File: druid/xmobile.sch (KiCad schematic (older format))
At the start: 33 parts, among them CON1 AVR-PDI-6, IC1 ATXMEGA128A4U-A, P1 CONN_4_miniUSB, P2 CONN_1, P3 CONN_8, P6 CONN_10, P7 CONN_4, Q1 A2SHB, Q2 A2SHB, SW1 SW_PUSH, U1 STF202-22T1G, U2 SIM800C

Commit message: - Переделана клавиатура - установлены все корпуса микросхем
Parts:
- removed P1: CONN_4_miniUSB, symbol CONN_4
- removed SW1: SW_PUSH, symbol SW_PUSH
- added P1: USB_B, usb:Conn_USBmicro-B_ebay-side_TH, symbol USB_B
- added U5: switch1, symbol switch1
- C1, C3: footprint (none) -> Capacitors_SMD:C_1206_HandSoldering; symbol C -> C-RESCUE-xmobile
- C2: footprint (none) -> Capacitors_SMD:c_elec_4x5.3; symbol CP1 -> CP1-RESCUE-xmobile
- D1: footprint (none) -> LEDs:LED_0603; symbol LED -> LED-RESCUE-xmobile
- IC1: symbol ATXMEGA128A4U-A -> ATXMEGA128A4U-A-RESCUE-xmobile
- L1: footprint (none) -> Inductors:Inductor_1212
- P3: footprint (none) -> Connectors_Molex:Molex_KK-6410-08_08x2.54mm_Straight
- P6: footprint (none) -> Connectors_Molex:Molex_KK-6410-06_06x2.54mm_Straight
- P7: footprint (none) -> Connectors_Molex:Molex_KK-6410-04_04x2.54mm_Straight
- R1, R2, R6: footprint Resistors_SMD:R_0402 -> Resistors_SMD:R_0603_HandSoldering; symbol R -> R-RESCUE-xmobile
- R10, R11, R12, R13, R14, R15, R16, R7, R8, R9: footprint (none) -> Resistors_SMD:R_0603_HandSoldering; symbol R -> R-RESCUE-xmobile
- R3, R4, R5: footprint Resistors_SMD:R_0402 -> Resistors_SMD:R_0603; symbol R -> R-RESCUE-xmobile
- U1: footprint MODULE -> semiconductor:TSOP-6
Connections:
- no-connect marks 1 -> 4

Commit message: Исправлины все ошибки и предупреждения в электрической схеме
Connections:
- net labels added: SIM_HOLDER_VDD_EXT
- net labels removed: GSM_VDD_EXT, XMEGA_RESET
- wire segments 41 -> 42
- no-connect marks 4 -> 13
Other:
- moved on the sheet: CON1, R6, U5
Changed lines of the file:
@@
 L R-RESCUE-xmobile R6
 U 1 1 5967CB22
-P 14100 4200
-F 0 "R6" V 14180 4200 40  0000 C CNN
-F 1 "10k" V 14107 4201 40  0000 C CNN
-F 2 "Resistors_SMD:R_0603_HandSoldering" V 14030 4200 30  0001 C CNN
-F 3 "" H 14100 4200 30  0000 C CNN
-	1    14100 4200
+P 14375 4725
+F 0 "R6" V 14455 4725 40  0000 C CNN
+F 1 "10k" V 14382 4726 40  0000 C CNN
+F 2 "Resistors_SMD:R_0603_HandSoldering" V 14305 4725 30  0001 C CNN
+F 3 "" H 14375 4725 30  0000 C CNN
+	1    14375 4725
 	-1   0    0    1
 $EndComp
@@
 Text Label 11200 7225 0    60   ~ 0
 GND
-Text Label 14100 3950 2    60   ~ 0
+Text Label 14375 4475 2    60   ~ 0
 3.3V
 $Comp
@@
 Text Label 9500 7675 2    60   ~ 0
 SIM_VDD
-Text Label 11200 6550 0    60   ~ 0
-GSM_VDD_EXT
 NoConn ~ 11200 6700
 Text Label 11200 7150 0    60   ~ 0
@@
 L AVR-PDI-6 CON1
 U 1 1 5AA047A2
-P 14650 4575
-F 0 "CON1" H 14570 4815 50  0000 C CNN
-F 1 "AVR-PDI-6" H 14440 4330 50  0000 L BNN
-F 2 "AVR-PDI-6" V 14205 4610 50  0001 C CNN
-F 3 "" H 14650 4575 60  0001 C CNN
-	1    14650 4575
-	1    0    0    -1
-$EndComp
-Text Label 14525 4675 2    60   ~ 0
-PDI_C
-Text Label 14775 4475 0    60   ~ 0
+P 14925 5100
+F 0 "CON1" H 14845 5340 50  0000 C CNN
+F 1 "AVR-PDI-6" H 14715 4855 50  0000 L BNN
+F 2 "AVR-PDI-6" V 14480 5135 50  0001 C CNN
+F 3 "" H 14925 5100 60  0001 C CNN
+	1    14925 5100
+	1    0    0    -1
+$EndComp
+Text Label 15050 5000 0    60   ~ 0
 3.3V
-Text Label 14775 4675 0    60   ~ 0
+Text Label 15050 5200 0    60   ~ 0
 GND
 Text Label 9000 2700 2    60   ~ 0
 PDI_D
 Wire Wire Line
-	14100 4450 14100 4925
-Wire Wire Line
-	13950 4475 14525 4475
+	14375 4975 14375 5450
 Text Label 8900 2600 2    60   ~ 0
-XMEGA_RESET
-Text Label 13950 4475 2    60   ~ 0
-XMEGA_RESET
-Connection ~ 14100 4475
-Text Label 13900 5625 3    60   ~ 0
+PDI_C
+Text Label 14175 6150 3    60   ~ 0
 GND
 $Sheet
@@
 L switch1 U5
 U 1 1 5AB790A5
-P 14000 5275
-F 0 "U5" H 14000 5075 60  0000 C CNN
-F 1 "switch1" H 14000 5475 60  0000 C CNN
-F 2 "" H 14000 5275 60  0001 C CNN
-F 3 "" H 14000 5275 60  0001 C CNN
-	1    14000 5275
-	0    1    1    0
-$EndComp
-Text Label 14000 5625 3    60   ~ 0
-GND
-NoConn ~ 14100 5625
-NoConn ~ 13900 4925
+P 14275 5800
+F 0 "U5" H 14275 5600 60  0000 C CNN
+F 1 "switch1" H 14275 6000 60  0000 C CNN
+F 2 "" H 14275 5800 60  0001 C CNN
+F 3 "" H 14275 5800 60  0001 C CNN
+	1    14275 5800
+	0    1    1    0
+$EndComp
+Text Label 14275 6150 3    60   ~ 0
+GND
+NoConn ~ 14375 6150
+NoConn ~ 14175 5450
 $Comp
 L USB_B P1
@@
 GND
 NoConn ~ 12975 4050
+NoConn ~ 15050 5100
+NoConn ~ 14800 5100
+Wire Wire Line
+	14225 5200 14800 5200
+Connection ~ 14375 5200
+Text Label 14800 5000 2    60   ~ 0
+PDI_D
+Text Label 14225 5200 2    60   ~ 0
+PDI_C
+$Comp
+L PWR_FLAG #FLG01
+U 1 1 5AB82AA2
+P 3050 1350
+F 0 "#FLG01" H 3050 1445 50  0001 C CNN
+F 1 "PWR_FLAG" H 3050 1530 50  0000 C CNN
+F 2 "" H 3050 1350 50  0000 C CNN
+F 3 "" H 3050 1350 50  0000 C CNN
+	1    3050 1350
+	1    0    0    -1
+$EndComp
+Wire Wire Line
+	2725 1350 3050 1350
+$Comp
+L PWR_FLAG #FLG02
+U 1 1 5AB83225
+P 10200 1500
+F 0 "#FLG02" H 10200 1595 50  0001 C CNN
+F 1 "PWR_FLAG" H 10200 1680 50  0000 C CNN
+F 2 "" H 10200 1500 50  0000 C CNN
+F 3 "" H 10200 1500 50  0000 C CNN
+	1    10200 1500
+	1    0    0    -1
+$EndComp
+NoConn ~ 11200 6400
+Text Label 11200 6850 0    60   ~ 0
+GND
+NoConn ~ 11200 7375
+NoConn ~ 11200 7450
+NoConn ~ 11200 7825
+NoConn ~ 11200 7900
+NoConn ~ 9500 7825
+NoConn ~ 9000 3550
+Text Label 3275 9525 0    60   ~ 0
+SIM_DET
+Text Label 2225 9425 2    60   ~ 0
+SIM_DATA
+Text Label 3275 9225 0    60   ~ 0
+SIM_CLK
+Text Label 2225 9325 2    60   ~ 0
+SIM_RST
+Text Label 2225 9225 2    60   ~ 0
+SIM_VDD
+Text Label 3275 9325 0    60   ~ 0
+GND
+Text Label 11200 6550 0    60   ~ 0
+SIM_HOLDER_VDD_EXT
+Text Label 3275 9425 0    60   ~ 0
+SIM_HOLDER_VDD_EXT
 $EndSCHEMATC

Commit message: Переместил посадочные места по кучкам
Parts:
- removed P2: CONN_1, symbol CONN_1
- added P2: CONN_01X02, Connectors_Hirose:Hirose_DF13-02P-1.25DS_02x1.25mm_Angled, symbol CONN_01X02
- CON1: footprint AVR-PDI-6 -> Connectors_JAE:JAE_LY20-06P-2T_2x03x2.00mm_Straight
- IC1: footprint TQFP44 -> tqfp:TQFP-44_10x10mm_Pitch0.8mm
- P3: footprint Connectors_Molex:Molex_KK-6410-08_08x2.54mm_Straight -> Connectors_JAE:JAE_LY20-08P-2T_2x04x2.00mm_Straight
- P6: footprint Connectors_Molex:Molex_KK-6410-06_06x2.54mm_Straight -> Connectors_Hirose:Hirose_DF13-10P-1.25DSA_10x1.25mm_Straight
- P7: footprint Connectors_Molex:Molex_KK-6410-04_04x2.54mm_Straight -> Connectors_JAE:JAE_LY20-04P-2T_2x02x2.00mm_Straight
- R3, R4, R5: footprint Resistors_SMD:R_0603 -> Resistors_SMD:R_0603_HandSoldering
- U2: footprint SIM800C:SIM800C -> SIM800C_lup:SIM800C
- U5: footprint (none) -> switch1:switch_6x9
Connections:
- no-connect marks 13 -> 14
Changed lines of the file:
@@
 F 0 "U2" H 10600 8175 60  0000 C CNN
 F 1 "SIM800C" H 9900 8175 60  0000 C CNN
-F 2 "SIM800C:SIM800C" H 10375 7400 60  0000 C CNN
+F 2 "SIM800C_lup:SIM800C" H 10375 7400 60  0000 C CNN
 F 3 "" H 10550 7200 60  0000 C CNN
 	1    10550 7200
@@
 F 0 "IC1" H 9200 4750 50  0000 L BNN
 F 1 "ATXMEGA128A4U-A" H 10150 2400 50  0000 L BNN
-F 2 "TQFP44" H 9350 2450 50  0001 C CNN
+F 2 "tqfp:TQFP-44_10x10mm_Pitch0.8mm" H 9350 2450 50  0001 C CNN
 F 3 "" H 9900 3600 60  0001 C CNN
 	1    9900 3600
@@
 F 0 "P3" V 14475 1975 60  0000 C CNN
 F 1 "CONN_8" V 14575 1975 60  0000 C CNN
-F 2 "Connectors_Molex:Molex_KK-6410-08_08x2.54mm_Straight" H 14525 1975 60  0001 C CNN
+F 2 "Connectors_JAE:JAE_LY20-08P-2T_2x04x2.00mm_Straight" H 14525 1975 60  0001 C CNN
 F 3 "" H 14525 1975 60  0001 C CNN
 F 4 "EPD display connector" V 14700 1975 60  0000 C CNN "description"
@@
 F 0 "R3" V 6255 7100 40  0000 C CNN
 F 1 "4.7KOmh" V 6182 7101 40  0000 C CNN
-F 2 "Resistors_SMD:R_0603" V 6105 7100 30  0001 C CNN
+F 2 "Resistors_SMD:R_0603_HandSoldering" V 6105 7100 30  0001 C CNN
 F 3 "" H 6175 7100 30  0000 C CNN
 	1    6175 7100
@@
 F 0 "R5" V 6905 6550 40  0000 C CNN
 F 1 "470Ом" V 6832 6551 40  0000 C CNN
-F 2 "Resistors_SMD:R_0603" V 6755 6550 30  0001 C CNN
+F 2 "Resistors_SMD:R_0603_HandSoldering" V 6755 6550 30  0001 C CNN
 F 3 "" H 6825 6550 30  0000 C CNN
 	1    6825 6550
@@
 F 0 "R4" V 6555 7425 40  0000 C CNN
 F 1 "4.7KOmh" V 6482 7426 40  0000 C CNN
-F 2 "Resistors_SMD:R_0603" V 6405 7425 30  0001 C CNN
+F 2 "Resistors_SMD:R_0603_HandSoldering" V 6405 7425 30  0001 C CNN
 F 3 "" H 6475 7425 30  0000 C CNN
 	1    6475 7425
@@
 Text Label 11200 7150 0    60   ~ 0
 GSM_ANT
-Text Label 5525 1875 2    60   ~ 0
+Text Label 5500 2225 2    60   ~ 0
 GSM_ANT
-$Comp
-L CONN_1 P2
-U 1 1 5A9488D3
-P 5675 1875
-F 0 "P2" H 5755 1875 40  0000 L CNN
-F 1 "CONN_1" H 5675 1930 30  0001 C CNN
-F 2 "" H 5675 1875 60  0001 C CNN
-F 3 "" H 5675 1875 60  0001 C CNN
-	1    5675 1875
-	1    0    0    -1
-$EndComp
 Connection ~ 10200 1500
 Wire Wire Line
@@
 F 0 "CON1" H 14845 5340 50  0000 C CNN
 F 1 "AVR-PDI-6" H 14715 4855 50  0000 L BNN
-F 2 "AVR-PDI-6" V 14480 5135 50  0001 C CNN
+F 2 "Connectors_JAE:JAE_LY20-06P-2T_2x03x2.00mm_Straight" V 14480 5135 50  0001 C CNN
 F 3 "" H 14925 5100 60  0001 C CNN
 	1    14925 5100
@@
 F 0 "P6" V 13275 3050 60  0000 C CNN
 F 1 "CONN_10" V 13375 3050 60  0000 C CNN
-F 2 "Connectors_Molex:Molex_KK-6410-06_06x2.54mm_Straight" H 13325 3050 60  0001 C CNN
+F 2 "Connectors_Hirose:Hirose_DF13-10P-1.25DSA_10x1.25mm_Straight" H 13325 3050 60  0001 C CNN
 F 3 "" H 13325 3050 60  0001 C CNN
 	1    13325 3050
@@
 F 0 "P7" V 13275 3900 50  0000 C CNN
 F 1 "CONN_4" V 13375 3900 50  0000 C CNN
-F 2 "Connectors_Molex:Molex_KK-6410-04_04x2.54mm_Straight" H 13325 3900 60  0001 C CNN
+F 2 "Connectors_JAE:JAE_LY20-04P-2T_2x02x2.00mm_Straight" H 13325 3900 60  0001 C CNN
 F 3 "" H 13325 3900 60  0001 C CNN
 	1    13325 3900
@@
 F 0 "U5" H 14275 5600 60  0000 C CNN
 F 1 "switch1" H 14275 6000 60  0000 C CNN
-F 2 "" H 14275 5800 60  0001 C CNN
+F 2 "switch1:switch_6x9" H 14275 5800 60  0001 C CNN
 F 3 "" H 14275 5800 60  0001 C CNN
 	1    14275 5800
@@
 PDI_C
 $Comp
-L PWR_FLAG #FLG01
+L PWR_FLAG #FLG1
 U 1 1 5AB82AA2
 P 3050 1350
-F 0 "#FLG01" H 3050 1445 50  0001 C CNN
+F 0 "#FLG1" H 3050 1445 50  0001 C CNN
 F 1 "PWR_FLAG" H 3050 1530 50  0000 C CNN
 F 2 "" H 3050 1350 50  0000 C CNN
@@
 	2725 1350 3050 1350
 $Comp
-L PWR_FLAG #FLG02
+L PWR_FLAG #FLG2
 U 1 1 5AB83225
 P 10200 1500
-F 0 "#FLG02" H 10200 1595 50  0001 C CNN
+F 0 "#FLG2" H 10200 1595 50  0001 C CNN
 F 1 "PWR_FLAG" H 10200 1680 50  0000 C CNN
 F 2 "" H 10200 1500 50  0000 C CNN
@@
 Text Label 3275 9425 0    60   ~ 0
 SIM_HOLDER_VDD_EXT
+$Comp
+L CONN_01X02 P2
+U 1 1 5AB8506D
+P 5700 2275
+F 0 "P2" H 5700 2425 50  0000 C CNN
+F 1 "CONN_01X02" V 5800 2275 50  0000 C CNN
+F 2 "Connectors_Hirose:Hirose_DF13-02P-1.25DS_02x1.25mm_Angled" H 5700 2275 50  0000 C CNN
+F 3 "" H 5700 2275 50  0000 C CNN
+	1    5700 2275
+	1    0    0    -1
+$EndComp
+NoConn ~ 5500 2325
 $EndSCHEMATC

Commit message: Заменил посадочные места для некоторых контактных расчёсок
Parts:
- P6: footprint Connectors_Hirose:Hirose_DF13-10P-1.25DSA_10x1.25mm_Straight -> Connectors_JAE:JAE_LY20-08P-2T_2x04x2.00mm_Straight
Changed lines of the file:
@@
 F 0 "P6" V 13275 3050 60  0000 C CNN
 F 1 "CONN_10" V 13375 3050 60  0000 C CNN
-F 2 "Connectors_Hirose:Hirose_DF13-10P-1.25DSA_10x1.25mm_Straight" H 13325 3050 60  0001 C CNN
+F 2 "Connectors_JAE:JAE_LY20-08P-2T_2x04x2.00mm_Straight" H 13325 3050 60  0001 C CNN
 F 3 "" H 13325 3050 60  0001 C CNN
 	1    13325 3050
@@
 PDI_C
 $Comp
-L PWR_FLAG #FLG1
+L PWR_FLAG #FLG01
 U 1 1 5AB82AA2
 P 3050 1350
-F 0 "#FLG1" H 3050 1445 50  0001 C CNN
+F 0 "#FLG01" H 3050 1445 50  0001 C CNN
 F 1 "PWR_FLAG" H 3050 1530 50  0000 C CNN
 F 2 "" H 3050 1350 50  0000 C CNN
@@
 	2725 1350 3050 1350
 $Comp
-L PWR_FLAG #FLG2
+L PWR_FLAG #FLG02
 U 1 1 5AB83225
 P 10200 1500
-F 0 "#FLG2" H 10200 1595 50  0001 C CNN
+F 0 "#FLG02" H 10200 1595 50  0001 C CNN
 F 1 "PWR_FLAG" H 10200 1680 50  0000 C CNN
 F 2 "" H 10200 1500 50  0000 C CNN

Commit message: зменена посадочная площадка (меньше чем была) лоя кондернасоторв 100n
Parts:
- C3: footprint Capacitors_SMD:C_1206_HandSoldering -> Capacitors_SMD:C_0603_HandSoldering
- P6: footprint Connectors_JAE:JAE_LY20-08P-2T_2x04x2.00mm_Straight -> Connectors_JAE:JAE_LY20-10P-2T_2x05x2.00mm_Straight
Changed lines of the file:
@@
 F 0 "C3" H 10800 2050 40  0000 L CNN
 F 1 "100n" H 10806 1865 40  0000 L CNN
-F 2 "Capacitors_SMD:C_1206_HandSoldering" H 10838 1800 30  0001 C CNN
+F 2 "Capacitors_SMD:C_0603_HandSoldering" H 10838 1800 30  0001 C CNN
 F 3 "" H 10800 1950 60  0000 C CNN
 	1    10800 1950
@@
 F 0 "P6" V 13275 3050 60  0000 C CNN
 F 1 "CONN_10" V 13375 3050 60  0000 C CNN
-F 2 "Connectors_JAE:JAE_LY20-08P-2T_2x04x2.00mm_Straight" H 13325 3050 60  0001 C CNN
+F 2 "Connectors_JAE:JAE_LY20-10P-2T_2x05x2.00mm_Straight" H 13325 3050 60  0001 C CNN
 F 3 "" H 13325 3050 60  0001 C CNN
 	1    13325 3050

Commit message: Соединеты проводникаи отдельные блоки и начато подключение SIM800 к XMEGA
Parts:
- removed C2: 10mk, Capacitors_SMD:c_elec_4x5.3, symbol CP1-RESCUE-xmobile
- removed C3: 100n, Capacitors_SMD:C_0603_HandSoldering, symbol C-RESCUE-xmobile
- removed IC1: ATXMEGA128A4U-A, tqfp:TQFP-44_10x10mm_Pitch0.8mm, symbol ATXMEGA128A4U-A-RESCUE-xmobile
- added C2, C3, C32, C33, C34, C35, C36, C37, C38, C39: 100nF, Capacitors_SMD:C_0603_HandSoldering, symbol C
- added C40, C41: 10mk, Capacitors_SMD:c_elec_4x5.3, symbol CP1-RESCUE-xmobile
- added IC1: ATXMEGA128A1U-A, tqfp:LQFP-100_14x14mm_Pitch0.5mm, symbol ATXMEGA128A1U-A
- added P10: CONN_01X08, Connectors_JAE:JAE_LY20-08P-2T_2x04x2.00mm_Straight, symbol CONN_01X08
- P2: footprint Connectors_Hirose:Hirose_DF13-02P-1.25DS_02x1.25mm_Angled -> Connectors_JAE:JAE_LY20-04P-2T_2x02x2.00mm_Straight
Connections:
- net 3.3V: now also C2.2, C3.2, C32.2, C33.2, C34.2, C35.2, C36.2, C37.2, IC1.14 (VCC), IC1.24 (VCC), IC1.34 (VCC), IC1.44 (VCC), IC1.54 (VCC), IC1.64 (VCC), IC1.74 (VCC), IC1.83 (VCC)
- net EPD_BUSY: now also IC1.98 (DAC1/AC3/ADC3/PA3)
- net EPD_CLK: now also IC1.22 (EVOUT/CLKP/SCK/TXD1/OC0DHS/PC7)
- net EPD_CS: now also IC1.19 (~SS~/~OC0CLS~/OC1A/PC4)
- net EPD_DC: now also IC1.96 (AC1/ADC1/PA1)
- net EPD_DIN: now also IC1.20 (MOSI/XCK1/OC0CHS/OC1B/PC5)
- net EPD_RST: now also IC1.99 (AC4/ADC4/PA4)
- net GND: now also C2.1, C3.1, C32.1, C33.1, C34.1, C35.1, C36.1, C37.1, C38.1, C39.2, C40.2, C41.2, IC1.13 (GND), IC1.23 (GND), IC1.3 (GND), IC1.33 (GND), IC1.43 (GND), IC1.53 (GND), IC1.63 (GND), IC1.73 (GND), IC1.84 (GND), IC1.93 (GND)
- net KBD_IN_1: now also IC1.30 (MOSI/XCK1/OC1B/PD5)
- net KBD_IN_2: now also IC1.31 (MISO/RXD1/D-/PD6)
- net KBD_IN_3: now also IC1.32 (EVOUT/CLKP/SCK/TXD1/D+/PD7)
- net KBD_OUT_1: now also IC1.15 (SDA/~OC0ALS~/OC0A/PC0)
- net KBD_OUT_2: now also IC1.16 (SCL/XCK0/OC0AHS/OC0B/PC1)
- net KBD_OUT_3: now also IC1.17 (RXD0/~OC0BLS~/OC0C/PC2)
- net PDI_C: now also IC1.90 (~RESET~/PDI_CLK)
- net PDI_D: now also IC1.89 (PDI_DAT)
- net XMEGA_PA0: now also IC1.95 (AREF/AC0/ADC0/PA0)
- net XMEGA_PA2: now also IC1.97 (DAC0/AC2/ADC2/PA2)
- net XMEGA_PA5: now also IC1.100 (AC5/ADC5/PA5)
- net XMEGA_PA6: now also IC1.1 (AC1OUT/AC6/ADC6/PA6)
- net XMEGA_PA7: now also IC1.2 (AC0OUT/AC7/ADC7/PA7)
- net XMEGA_PB0: now also IC1.5 (AREF/AC0/ADC0/PB0)
- net XMEGA_PB1: now also IC1.6 (AC1/ADC1/PB1)
- net XMEGA_PB2: now also IC1.7 (DAC0/AC2/ADC2/PB2)
- net XMEGA_PB3: now also IC1.8 (DAC1/AC3/ADC3/PB3)
- net XMEGA_PC3: now also IC1.18 (TXD0/OC0BHS/OC0D/PC3)
- net XMEGA_PC6: now also IC1.21 (CLKRTC/MISO/RXD1/~OC0DLS~/PC6)
- net XMEGA_PD0_GSM_POWER: now also IC1.25 (SDA/OC0A/PD0)
- net XMEGA_PD1_GPIO: now also IC1.26 (SCL/XCK0/OC0B/PD1)
- net XMEGA_PD2_GPIO: now also IC1.27 (RXD0/OC0C/PD2)
- net XMEGA_PD3_GPIO: now also IC1.28 (TXD0/OC0D/PD3)
- net XMEGA_PD4_GPIO: now also IC1.29 (~SS~/OC1A/PD4)
- net XMEGA_PE0_GPIO: now also IC1.35 (SDA/~OC0ALS~/OC0A/PE0)
- net XMEGA_PE2_RXD0: now also IC1.37 (RXD0/~OC0BLS~/OC0C/PE2)
- net XMEGA_PE3_TXD0: now also IC1.38 (TXD0/OC0BHS/OC0D/PE3)
- net XMEGA_PR0: now also IC1.91 (PR0/XTAL2)
- net XMEGA_PR1: now also IC1.92 (PR1/XTAL1)
- net at L1.1: now also C38.2, C39.1, C40.1, C41.1, IC1.4 (AVCC), IC1.94 (AVCC)
- new net: IC1.45 (PF0/OC0A/SDA), P10.8 (P8)
- new net: IC1.46 (PF1/OC0B/SCL/XCK0), P10.7 (P7)
- new net: IC1.47 (PF2/OC0C/RXD0), P10.6 (P6)
- new net: IC1.48 (PF3/OC0D/TXD0), P10.5 (P5)
- new net: IC1.49 (PF4/OC1A/~SS~), P10.4 (P4)
- new net: IC1.50 (PF5/OC1B/MOSI/XCK1), P10.3 (P3)
- new net: IC1.51 (PF6/MISO/RXD1), P10.2 (P2)
- new net: IC1.52 (PF7/SCK/TXD1), P10.1 (P1)
- no-connect marks 14 -> 50
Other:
- moved on the sheet: D1, P2, P3, P6, P7, Q2, R3, R4, R5, U2

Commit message: Всё разведено кроме земель. Площидки надо проверять.
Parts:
- removed P6: CONN_10, Connectors_JAE:JAE_LY20-10P-2T_2x05x2.00mm_Straight, symbol CONN_10
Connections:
- net XMEGA_PA5: no longer names the net of IC1.100 (AC5/ADC5/PA5)
- net XMEGA_PA6: no longer names the net of IC1.1 (AC1OUT/AC6/ADC6/PA6)
- net XMEGA_PA7: no longer names the net of IC1.2 (AC0OUT/AC7/ADC7/PA7)
- net XMEGA_PB0: no longer names the net of IC1.5 (AREF/AC0/ADC0/PB0)
- net XMEGA_PB1: no longer names the net of IC1.6 (AC1/ADC1/PB1)
- net XMEGA_PB2: no longer names the net of IC1.7 (DAC0/AC2/ADC2/PB2)
- net XMEGA_PB3: no longer names the net of IC1.8 (DAC1/AC3/ADC3/PB3)
- net XMEGA_PC3: no longer names the net of IC1.18 (TXD0/OC0BHS/OC0D/PC3)
- net XMEGA_PR0: no longer names the net of IC1.91 (PR0/XTAL2)
- net XMEGA_PR1: no longer names the net of IC1.92 (PR1/XTAL1)
- no-connect marks 50 -> 60
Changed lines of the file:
@@
 XMEGA_PD0_GSM_POWER
-$Comp
-L CONN_10 P6
-U 1 1 5AA653CA
-P 15300 2975
-F 0 "P6" V 15250 2975 60  0000 C CNN
-F 1 "CONN_10" V 15350 2975 60  0000 C CNN
-F 2 "Connectors_JAE:JAE_LY20-10P-2T_2x05x2.00mm_Straight" H 15300 2975 60  0001 C CNN
-F 3 "" H 15300 2975 60  0001 C CNN
-	1    15300 2975
-	1    0    0    -1
-$EndComp
-Text Label 10550 2975 0    60   ~ 0
-XMEGA_PA5
-Text Label 14950 2525 2    60   ~ 0
-XMEGA_PA5
-Text Label 10550 3075 0    60   ~ 0
-XMEGA_PA6
-Text Label 14950 2625 2    60   ~ 0
-XMEGA_PA6
-Text Label 10550 3175 0    60   ~ 0
-XMEGA_PA7
-Text Label 14950 2725 2    60   ~ 0
-XMEGA_PA7
-Text Label 10550 3325 0    60   ~ 0
-XMEGA_PB0
-Text Label 14950 2825 2    60   ~ 0
-XMEGA_PB0
-Text Label 10550 3425 0    60   ~ 0
-XMEGA_PB1
-Text Label 14950 2925 2    60   ~ 0
-XMEGA_PB1
-Text Label 10550 3525 0    60   ~ 0
-XMEGA_PB2
-Text Label 14950 3025 2    60   ~ 0
-XMEGA_PB2
-Text Label 10550 3625 0    60   ~ 0
-XMEGA_PB3
-Text Label 14950 3125 2    60   ~ 0
-XMEGA_PB3
-Text Label 10550 4475 0    60   ~ 0
-XMEGA_PC3
-Text Label 14950 3225 2    60   ~ 0
-XMEGA_PC3
-Text Label 8150 2725 2    60   ~ 0
-XMEGA_PR0
-Text Label 14950 3325 2    60   ~ 0
-XMEGA_PR0
-Text Label 14950 3425 2    60   ~ 0
-XMEGA_PR1
 $Comp
 L CONN_4 P7
@@
 Text Label 14950 3775 2    60   ~ 0
 XMEGA_PA2
-Text Label 8150 2825 2    60   ~ 0
-XMEGA_PR1
 Text Label 10550 4775 0    60   ~ 0
 XMEGA_PC6
@@
 	1    0    0    -1
 $EndComp
+NoConn ~ 10550 3075
+NoConn ~ 10550 2975
+NoConn ~ 10550 3525
+NoConn ~ 10550 3625
+NoConn ~ 10550 3175
+NoConn ~ 10550 3325
+NoConn ~ 10550 3425
+NoConn ~ 8150 2725
+NoConn ~ 8150 2825
+NoConn ~ 10550 4475
 $EndSCHEMATC

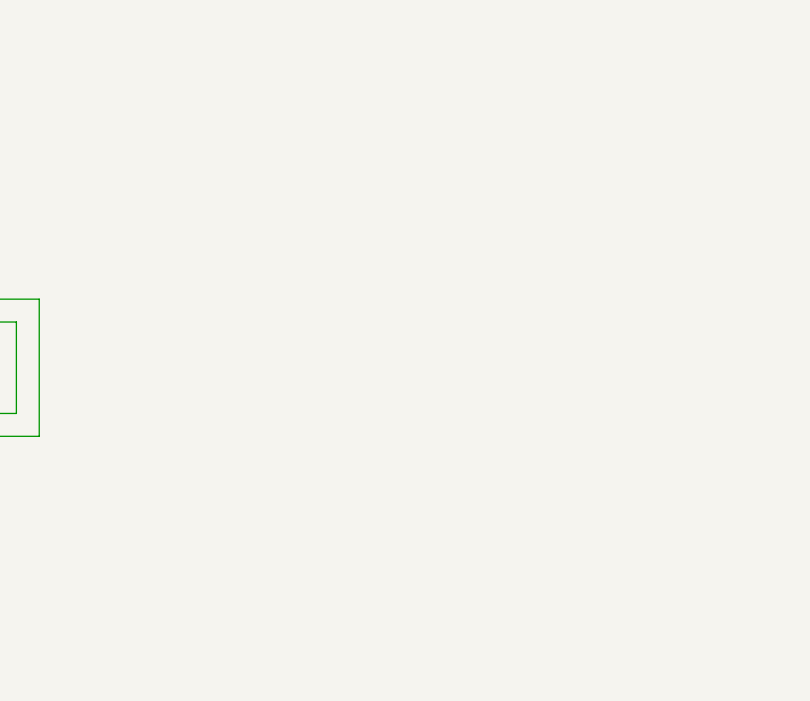
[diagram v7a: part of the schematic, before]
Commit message: [HW] Add SRAM component library
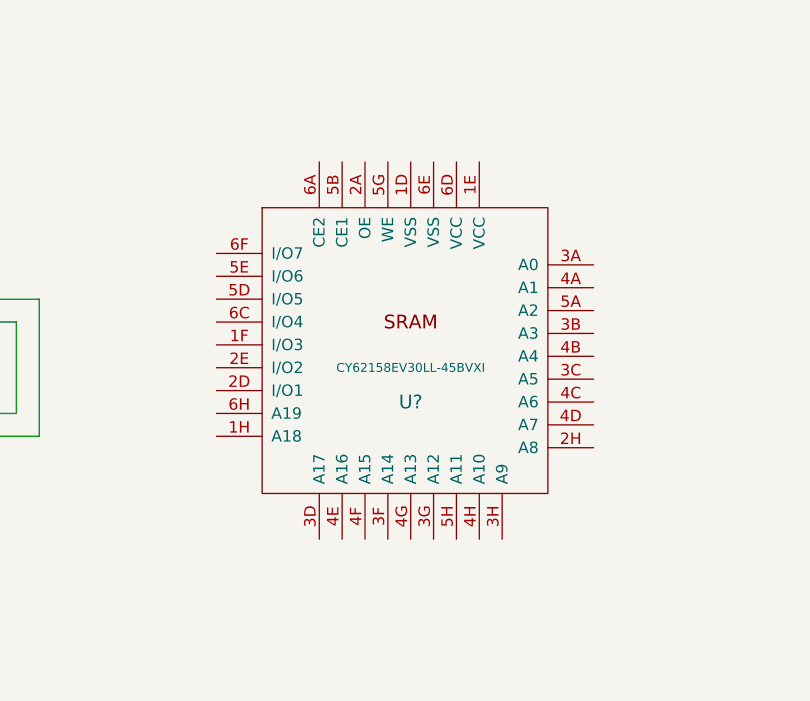
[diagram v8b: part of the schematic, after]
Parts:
- added U?: CY62158EV30LL-45BVXI, symbol CY62158EV30LL-45BVXI
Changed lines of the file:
@@
 LIBS:MCP73871
 LIBS:switch1
+LIBS:SRAM
 LIBS:xmobile-cache
 EELAYER 25 0
@@
 NoConn ~ 8150 2825
 NoConn ~ 10550 4475
+$Comp
+L CY62158EV30LL-45BVXI U?
+U 1 1 5C118522
+P 5500 4600
+F 0 "U?" H 5500 4400 60  0000 C CNN
+F 1 "CY62158EV30LL-45BVXI" H 5500 4550 39  0000 C CNN
+F 2 "" H 5550 3650 60  0000 C CNN
+F 3 "" H 5550 3650 60  0000 C CNN
+	1    5500 4600
+	1    0    0    -1
+$EndComp
 $EndSCHEMATC
